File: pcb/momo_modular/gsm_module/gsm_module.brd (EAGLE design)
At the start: 50.8 x 33 mm, 19 parts, among them U1 PIC16LF1823, U2 TI-HIGHSIDE-PFET, U3 SIM900, U4 ESD-SMF05C

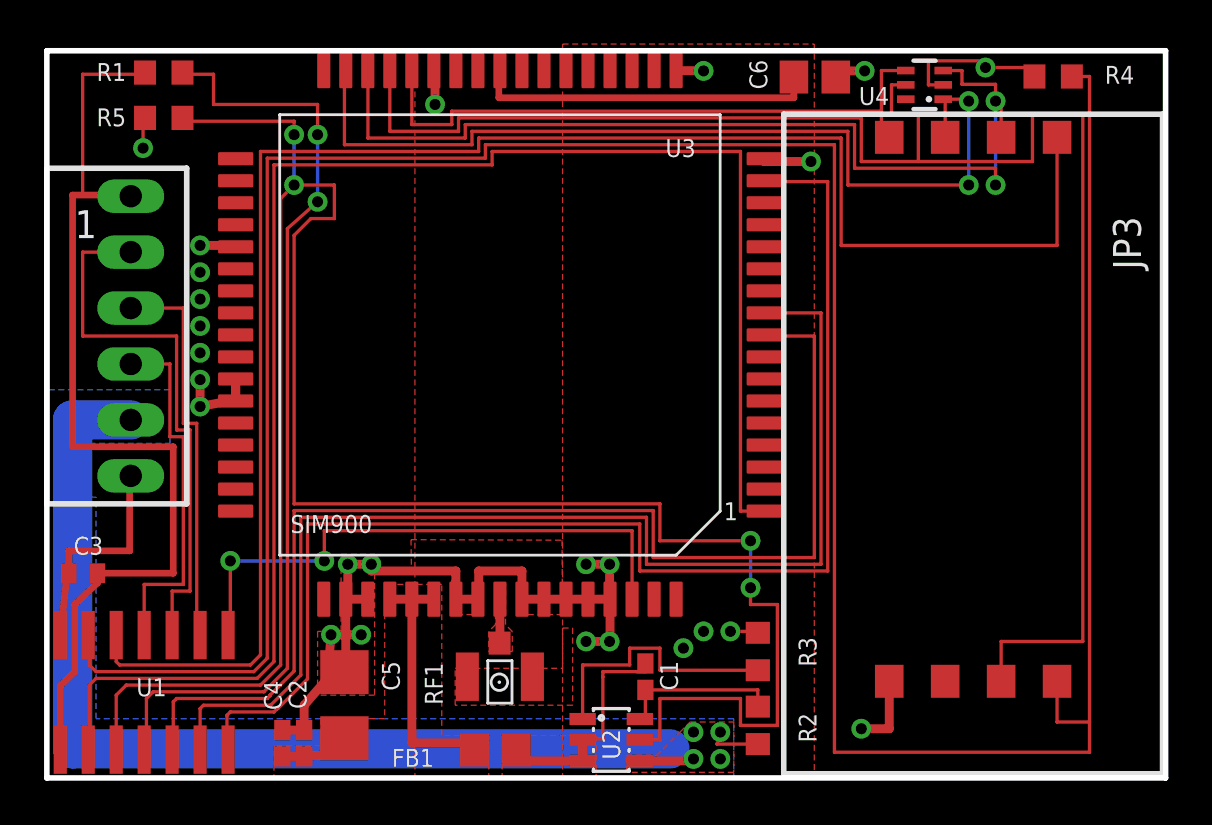
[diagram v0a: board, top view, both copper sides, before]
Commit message: Revise GSM module to include pic16lf1847, microsim
Also updated layout for better reflow and moved
traces further from board edges.
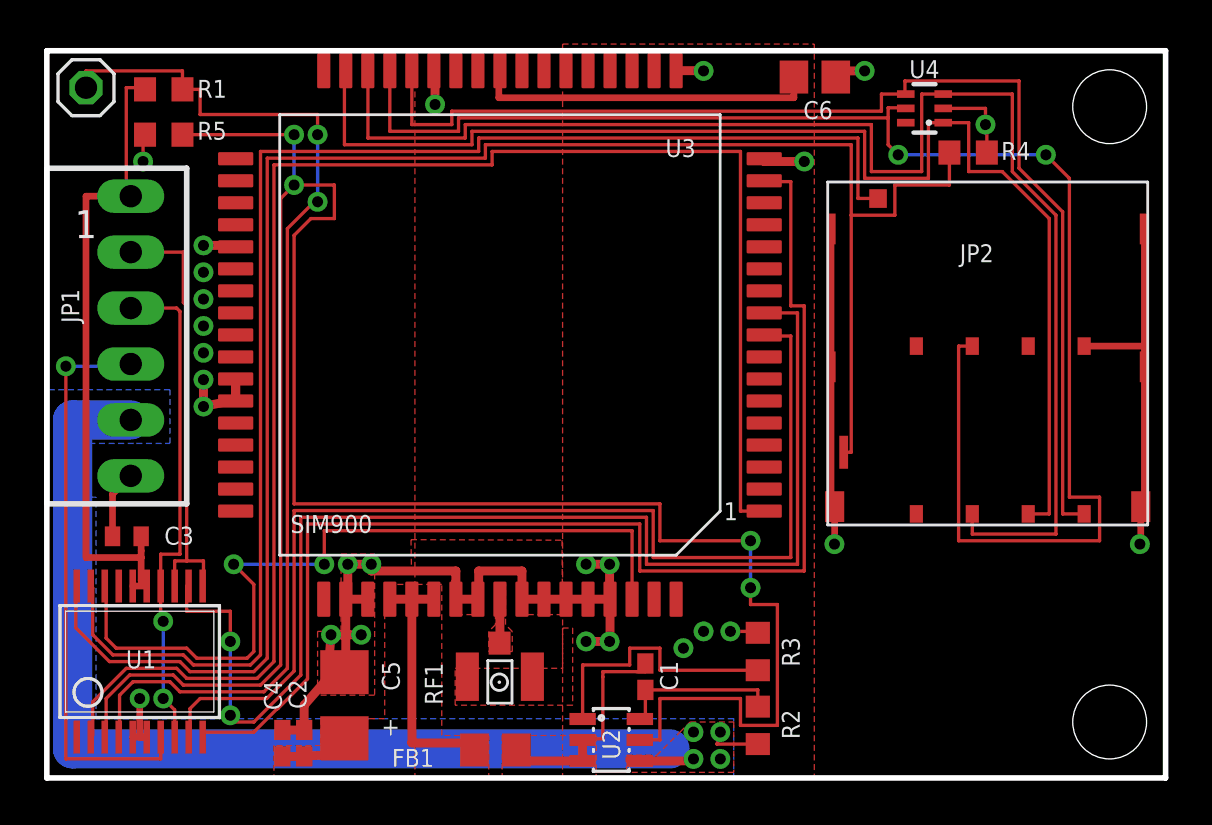
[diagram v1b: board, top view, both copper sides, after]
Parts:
- added JP2: SIMHOLDER-8PINMICROSIM, components:MOLEX-MICROSIM-0787270001
- JP3: value SIMHOLDER-8PINHING -> (none); device components:CCM03-SIMHOLDER -> pinhead:1X01
- U1: value PIC16LF1823 -> PIC16LF1847; device components:SO14 -> components:SSOP20
- moved JP3 42.9 mm to (6.86, 36.4), turned to 0 degrees
- moved R4 5.18 mm to (46.9, 33.5), turned to 180 degrees
- moved C3 2.60 mm to (8.71, 16.1)
- moved U1 1.41 mm to (9.30, 10.4)
- moved U4 1.07 mm to (44.9, 35.5)
- moved R1 0.76 mm to (10.4, 36.3)
- moved R5 0.76 mm to (10.4, 34.3)
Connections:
- removed net N$6: R1.1, U1.4
- new net N$2: JP3.1, R1.1, U1.4
- net ALARM: now also U1.7; no longer U1.11
- net CLOCK: now also U1.11, U1.13; no longer U1.10
- net DAT: now also U1.14, U1.8; no longer U1.9
- net GND: now also JP2.C5, JP2.GND1, JP2.GND2, JP2.GND3, JP2.GND4, JP2.GND5, JP2.GND6, U1.5, U1.6; no longer JP3.GND, U1.14
- net RESET: now also U1.10; no longer U1.7
- net RXD: now also U1.12; no longer U1.6
- net SIMCLK: now also JP2.C3; no longer JP3.CLOCK
- net SIMDAT: now also JP2.C7; no longer JP3.IO
- net SIMRST: now also JP2.C2; no longer JP3.RESET
- net SIMVCC: now also JP2.C1; no longer JP3.VCC
- net STATUS: now also U1.18; no longer U1.8
- net SW1: now also JP2.DCONT, U1.19; no longer JP3.SW1, U1.12
- net SW2: now also JP2.DSPRING, U1.20; no longer JP3.SW2, U1.13
- net TXD: now also U1.9; no longer U1.5
- net VCCINT: now also U1.15, U1.16; no longer U1.1
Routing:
- net SW2: track 132.9 -> 83.3 mm
- net N$2: track 0.00 -> 49.5 mm, vias 0 -> 2
- net N$6: track 43.1 -> 0.00 mm, vias 2 -> 0
- net SIMVCC: track 28.9 -> 53.5 mm
- net GND: track 71.4 -> 91.2 mm, vias 25 -> 27
- net SIMCLK: track 44.4 -> 64.1 mm, vias 2 -> 0
- net VCCINT: track 47.7 -> 29.8 mm
- net SIMRST: track 41.8 -> 58.2 mm, vias 2 -> 0
- net SW1: track 77.4 -> 64.9 mm
- net STATUS: track 26.1 -> 36.7 mm
- net ALARM: track 16.5 -> 26.2 mm, vias 0 -> 1
- net CLOCK: track 25.3 -> 20.1 mm
- net DAT: track 17.9 -> 22.8 mm, vias 0 -> 2
- net TXD: track 53.7 -> 50.1 mm
- net RXD: track 54.0 -> 57.1 mm, vias 0 -> 2
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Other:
- board text added: "+"
